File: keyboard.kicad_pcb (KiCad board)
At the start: 2 copper layers, 284.5 x 94 mm, 156 parts, among them J1 Conn_SWD, J2 Conn_ETM, J3 USB_C_Receptacle, J4 JST_PH, J5 PicoBlade, J6 PicoBlade, J7 2.54mm, J8 PicoBlade, J9 PicoBlade, Q1 IRLML2502, Q2 FDC6312P, SW1 Slide Switch, U1 BL653, U2 BQ24295, U3 MCP73832-2-MC, U4 MCP1811AT-033/OT, Y1 32.768kHz

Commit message: all routed
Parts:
- moved C1 9.71 mm to (154.3, 121.9)
- moved Y1 7.73 mm to (157.5, 121.9)
- moved C2 6.02 mm to (160.7, 121.9)
- moved C4 4.26 mm to (168.9, 122.6), turned to 90 degrees
- moved C3 3.86 mm to (171.4, 122.6), turned to 90 degrees
- moved D22 0.65 mm to (78.7, 113.4)
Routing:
- net GND: track 776.6 -> 1183.8 mm, vias 58 -> 168
- net /row2: track 0.00 -> 399.0 mm, vias 0 -> 6
- net /row5: track 0.83 -> 329.5 mm, vias 1 -> 6
- net /col2: track 14.2 -> 322.0 mm, vias 1 -> 8
- net /row4: track 0.79 -> 285.3 mm, vias 1 -> 8
- net /row1: track 32.0 -> 309.0 mm, vias 2 -> 4
- net /col14: track 0.00 -> 275.5 mm, vias 0 -> 3
- net /row3: track 0.79 -> 273.5 mm, vias 1 -> 4
- net /col13: track 0.81 -> 247.4 mm, vias 1 -> 3
- net /col1: track 0.00 -> 242.2 mm, vias 0 -> 3
- net /col12: track 0.79 -> 235.8 mm, vias 1 -> 3
- net /col11: track 1.37 -> 221.9 mm, vias 1 -> 4
- net /col10: track 0.81 -> 198.5 mm, vias 1 -> 3
- net /CAPS_LED: track 0.00 -> 193.8 mm, vias 0 -> 2
- net /Power/NTC: track 4.81 -> 193.4 mm, vias 0 -> 2
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
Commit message: almost ready rev a
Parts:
- D1, D10, D11, D12, D13, D14, D15, D16, D17, D18, D19, D2, D20, D21, D22, D23, D24, D25, D26, D27, D28, D29, D3, D30, D31, D32, D33, D4, D5, D6, D7, D8, D9: value D_Dual_CommonAnode_KKA_Split -> BAS70-06
- R6: value 2k -> 1k
- moved D22 10.2 mm to (88.9, 113.4)
- moved R4 3.81 mm to (61.0, 64.1), turned to 180 degrees
- moved D14 3.57 mm to (304.8, 75.3)
- moved R5 1.91 mm to (64.8, 64.1)
- moved C6 0.90 mm to (86.4, 57.1)
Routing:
- net GND: track 1183.8 -> 1209.5 mm, vias 168 -> 171
- net Net-(D22-Pad2): track 21.3 -> 11.1 mm
- net Net-(D22-Pad1): track 5.40 -> 15.6 mm
- net /row4: track 285.3 -> 275.2 mm
- net Net-(J3-PadA5): track 9.36 -> 13.3 mm
- net /row2: track 399.0 -> 395.1 mm
- net Net-(D14-Pad1): track 6.71 -> 2.86 mm
- net Net-(J3-PadB5): track 13.9 -> 10.1 mm
- net Net-(D14-Pad2): track 16.6 -> 19.1 mm

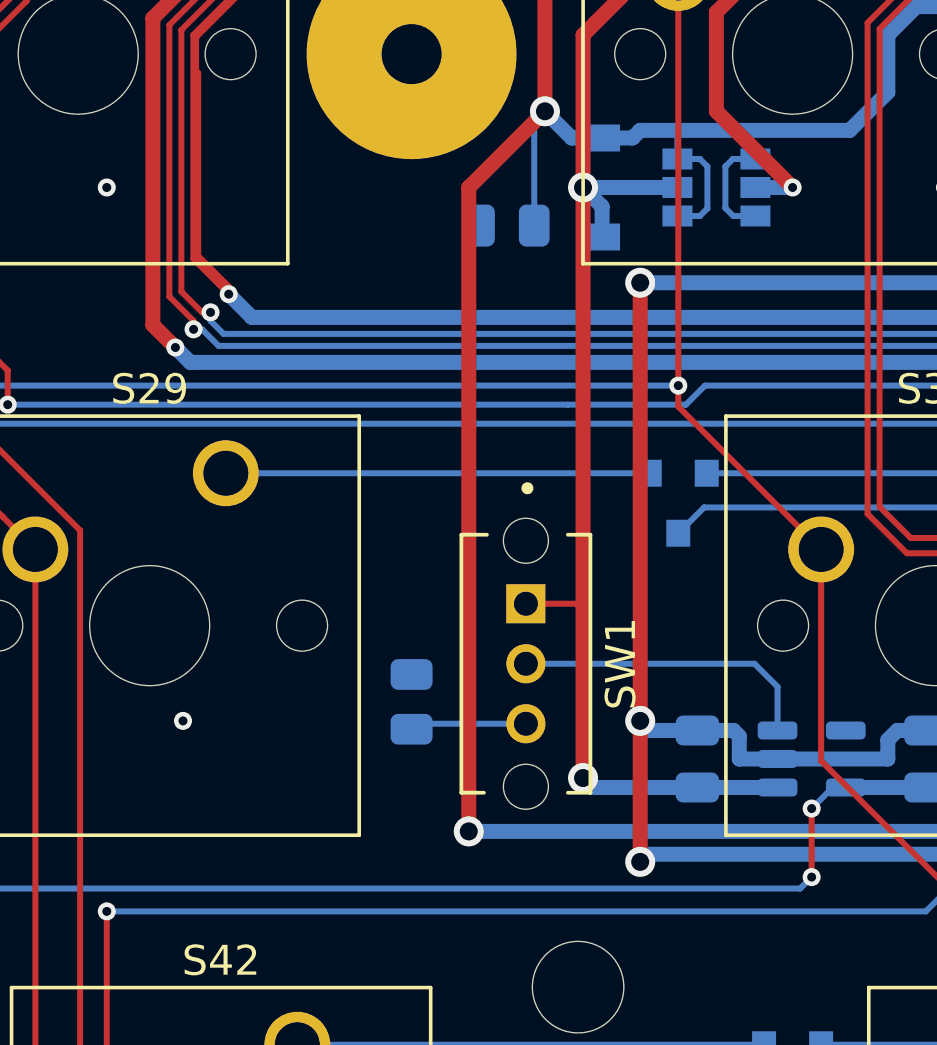
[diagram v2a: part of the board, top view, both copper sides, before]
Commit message: improve power switch circuit
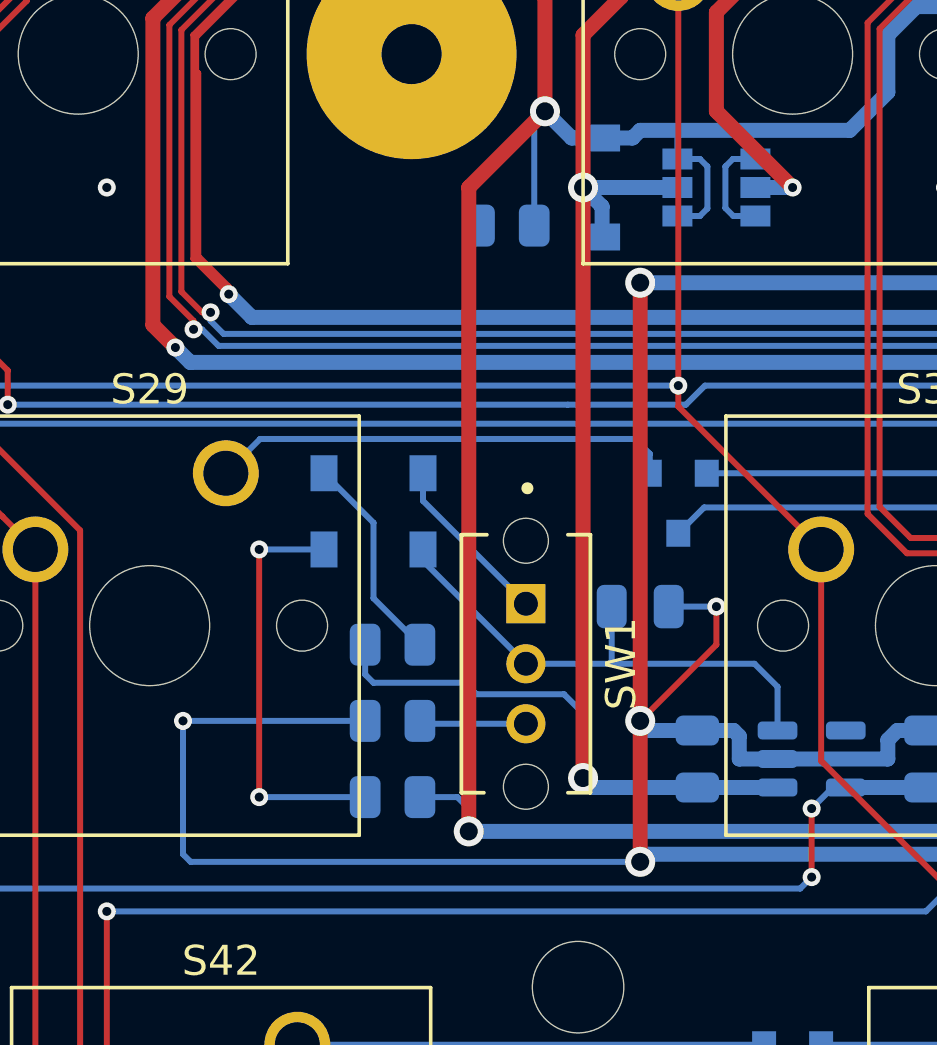
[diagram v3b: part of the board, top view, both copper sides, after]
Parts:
- added C16: 1uF, Capacitor_SMD:C_0805_2012Metric, B.Cu at (83.8, 97.8)
- added D35: 1N4007, Diode_SMD:D_SOD-123, B.Cu at (74.9, 93.3)
- added D36: 1N4007, Diode_SMD:D_SOD-123, B.Cu at (74.9, 95.9)
- added R15: 100k, Resistor_SMD:R_0805_2012Metric, B.Cu at (75.6, 99.1)
- added R16: 100k, Resistor_SMD:R_0805_2012Metric, B.Cu at (75.6, 101.6)
- D34: value ~ -> 1N4007
- Q1: value IRLML2502 -> 2N7002
- moved R11 3.24 mm to (75.6, 104.1), turned to 180 degrees
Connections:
- net /Power/PWROFF renamed /PWRON
- R11 pad 1: GND -> VBUS
- R11 pad 2: Net-(R11-Pad2) -> Net-(D36-Pad2)
- SW1 pad 1: VSYS -> Net-(D35-Pad1)
- SW1 pad 3: Net-(R11-Pad2) -> Net-(R16-Pad2)
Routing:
- net GND: track 1209.5 -> 1241.8 mm, vias 171 -> 172
- net Net-(D36-Pad2): track 0.00 -> 13.9 mm, vias 0 -> 2
- net VSYS: track 64.6 -> 73.8 mm
- net /PWRON: track 10.2 -> 17.3 mm
- net Net-(D35-Pad2): track 0.00 -> 7.04 mm
- net Net-(D35-Pad1): track 0.00 -> 5.77 mm
- net Net-(R11-Pad2): track 4.43 -> 0.00 mm
- net Net-(R16-Pad2): track 0.00 -> 3.57 mm
- net VBUS: track 280.9 -> 283.4 mm
- net Net-(D15-Pad1): track 14.1 -> 15.5 mm

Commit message: final changes to power switch circuitry
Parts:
- removed R11: 10k, Resistor_SMD:R_0805_2012Metric
- R15, R16: value 100k -> 10k
- TH1: value 10k -> 10k NTC
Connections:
- D36 pad 2: Net-(D36-Pad2) -> VBUS
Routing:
- net Net-(D36-Pad2): track 13.9 -> 0.00 mm, vias 2 -> 0
- net GND: track 1241.8 -> 1229.5 mm, vias 172 -> 173
- net VBUS: track 283.4 -> 285.5 mm, vias 12 -> 13
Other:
- board text added: "BLU64 Mechanical Keyboard Designed by Andrew Chen github.com/andrewcchen/blu64 Licensed under CERN-OHL-S v2 or any later version"

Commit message: Rev A complete
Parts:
- added LED3: Red, LED_THT:LED_D3.0mm, F.Cu at (57.8, 99.7)
- S1, S10, S11, S12, S13, S14, S15, S16, S17, S18, S19, S2, S20, S21, S22, S23, S24, S25, S26, S27, S28, S29, S3, S30, S31, S32, S33, S34, S35, S36, S37, S38, S39, S4, S40, S41, S42, S43, S44, S45, S46, S47, S48, S49, S5, S50, S51, S52, S53, S54, S55, S56, S57, S58, S59, S6, S60, S61, S62, S63, S64, S7, S8, S9: value SW_Push -> MX1A
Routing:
- net +3V3: track 236.5 -> 247.0 mm
- net Net-(LED2-Pad1): track 1.96 -> 7.91 mm, vias 1 -> 0
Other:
- board text added: "BLU64 Keyboard Rev A Designed by Andrew Chen github.com/andrewcchen/blu64 Licensed under CERN-OHL-S v2 or any later version"
- board text removed: "BLU64 Mechanical Keyboard Designed by Andrew Chen github.com/andrewcchen/blu64 Licensed under CERN-OHL-S v2 or any later version"

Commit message: Change diode part BAS70 -> BAT54
Use lower voltage diode for better forward voltage
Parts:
- D1, D10, D11, D12, D13, D14, D15, D16, D17, D18, D19, D2, D20, D21, D22, D23, D24, D25, D26, D27, D28, D29, D3, D30, D31, D32, D33, D4, D5, D6, D7, D8, D9: value BAS70-06 -> BAT54A

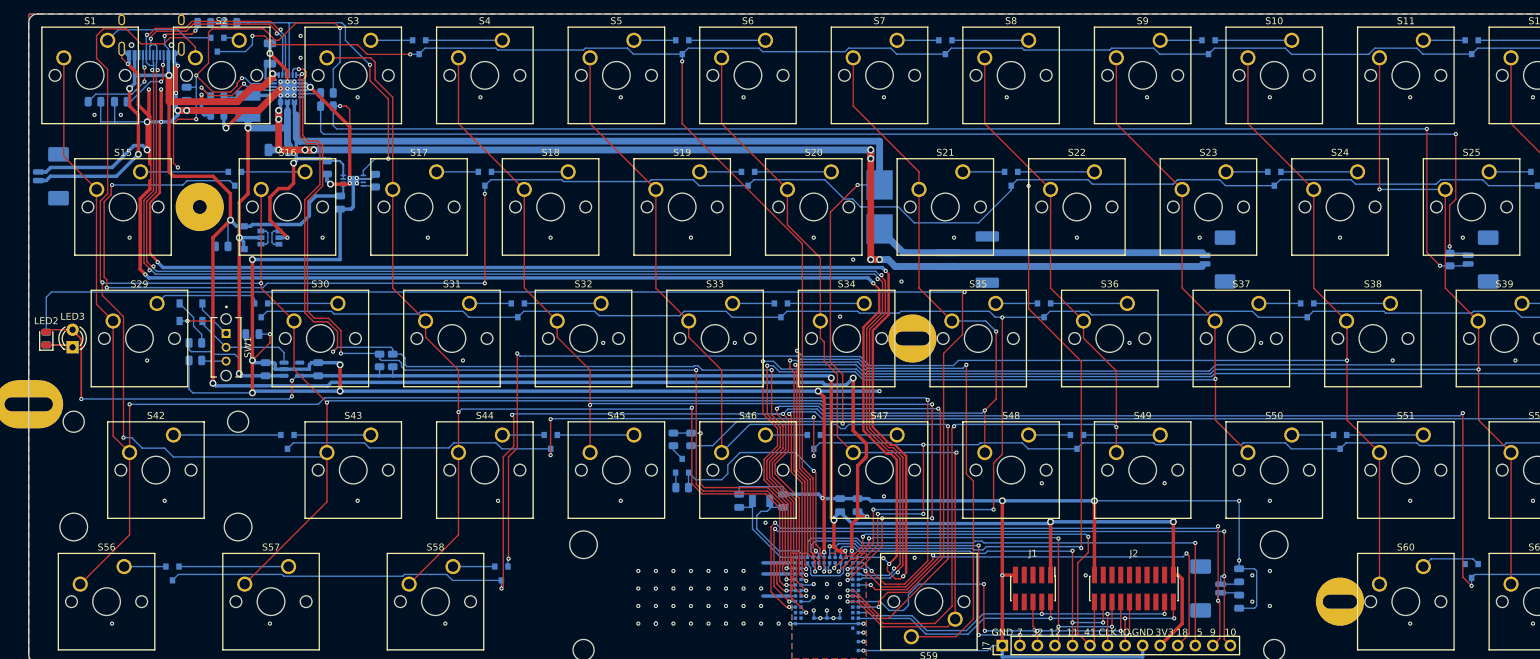
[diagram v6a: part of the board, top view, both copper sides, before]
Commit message: oops switch on wrong side of board
only affects silkscreen
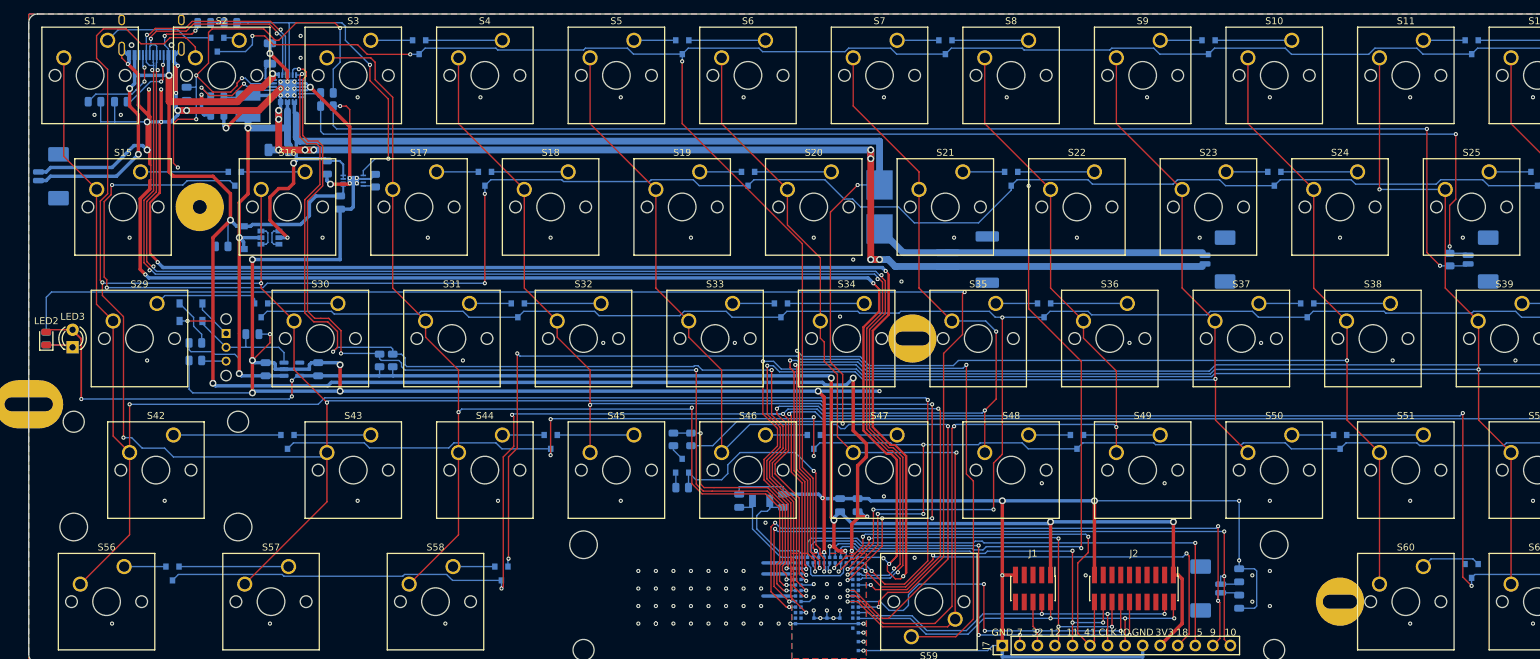
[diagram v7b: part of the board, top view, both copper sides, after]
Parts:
- SW1: moved to B.Cu

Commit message: Fix battery sense quiescent current draw
Q1 was useless because current still sinks through the mcu's esd diodes
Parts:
- removed Q1: 2N7002, Package_TO_SOT_SMD:SOT-23
- removed R3: 10k, Resistor_SMD:R_0805_2012Metric
- added C17: 100nF, Capacitor_SMD:C_0805_2012Metric, B.Cu at (146.1, 116.2)
- R1, R2: value 10k 1% -> 1M 1%
- moved C16 0.64 mm to (84.5, 97.8)
- turned R1 to 270 degrees
- turned R2 to 90 degrees
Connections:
- D21 pad 1: Net-(D21-Pad1) -> (no net)
- D31 pad 1: Net-(D31-Pad1) -> (no net)
- J1 pad 10: Net-(J1-Pad10) -> (no net)
- J1 pad 7: Net-(J1-Pad7) -> (no net)
- J1 pad 8: Net-(J1-Pad8) -> (no net)
- J2 pad 10: Net-(J2-Pad10) -> (no net)
- J2 pad 11: Net-(J2-Pad11) -> (no net)
- J2 pad 13: Net-(J2-Pad13) -> (no net)
- J2 pad 6: Net-(J2-Pad6) -> (no net)
- J2 pad 7: Net-(J2-Pad7) -> (no net)
- J2 pad 8: Net-(J2-Pad8) -> (no net)
- J3 pad A8: Net-(J3-PadA8) -> (no net)
- J3 pad B8: Net-(J3-PadB8) -> (no net)
- J7 pad 12: /P5 -> /P4
- J7 pad 13: /NFC1 -> /P5
- J7 pad 14: /NFC2 -> /P40
- R2 pad 2: Net-(Q1-Pad3) -> GND
- U1 pad 2: Net-(U1-Pad2) -> (no net)
- U1 pad 22: Net-(U1-Pad22) -> (no net)
- U1 pad 34: /BAT_SENS_EN -> /P4
- U1 pad 4: Net-(U1-Pad4) -> (no net)
- U1 pad 44: Net-(U1-Pad44) -> (no net)
- U1 pad 63: Net-(U1-Pad63) -> (no net)
- U1 pad 64: Net-(U1-Pad64) -> (no net)
- U2 pad 12: Net-(U2-Pad12) -> (no net)
- U2 pad 7: Net-(U2-Pad7) -> (no net)
- U4 pad 4: Net-(U4-Pad4) -> (no net)
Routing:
- net /P40: track 1.42 -> 91.4 mm, vias 1 -> 3
- net /P4: track 0.00 -> 88.4 mm, vias 0 -> 3
- net /BAT_SENS_EN: track 40.8 -> 0.00 mm, vias 2 -> 0
- net Net-(C8-Pad2): track 70.0 -> 55.1 mm, vias 5 -> 3
- net GND: track 1229.5 -> 1242.0 mm, vias 173 -> 170
- net /NFC2: track 99.0 -> 87.6 mm
- net /NFC1: track 101.2 -> 94.1 mm
- net Net-(Q1-Pad3): track 2.42 -> 0.00 mm
- net /P5: track 73.9 -> 76.3 mm
- net VBUS: track 285.5 -> 283.6 mm
- net /BAT_SENS: track 37.3 -> 35.7 mm
- net /row5: track 329.5 -> 328.0 mm
- net /row3: track 273.5 -> 274.8 mm
- net /row4: track 275.2 -> 276.1 mm
- net /P12: track 62.8 -> 63.7 mm
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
